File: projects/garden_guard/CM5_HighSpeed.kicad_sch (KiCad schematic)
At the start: 29 parts, among them J14 JST_SHBM04B-SRSS-TB, J2 Conn_02x07_Odd_Even, J3 Conn_01x03, J7 Micro_SD_Card_Det, J8 THD-20-R, J9 THD-02-R, SW1 Tact button, U1 TPD4EUSB30, U18 RT9742GGJ5, U2 TPD4EUSB30, U3 MagJack-A70-112-331N126

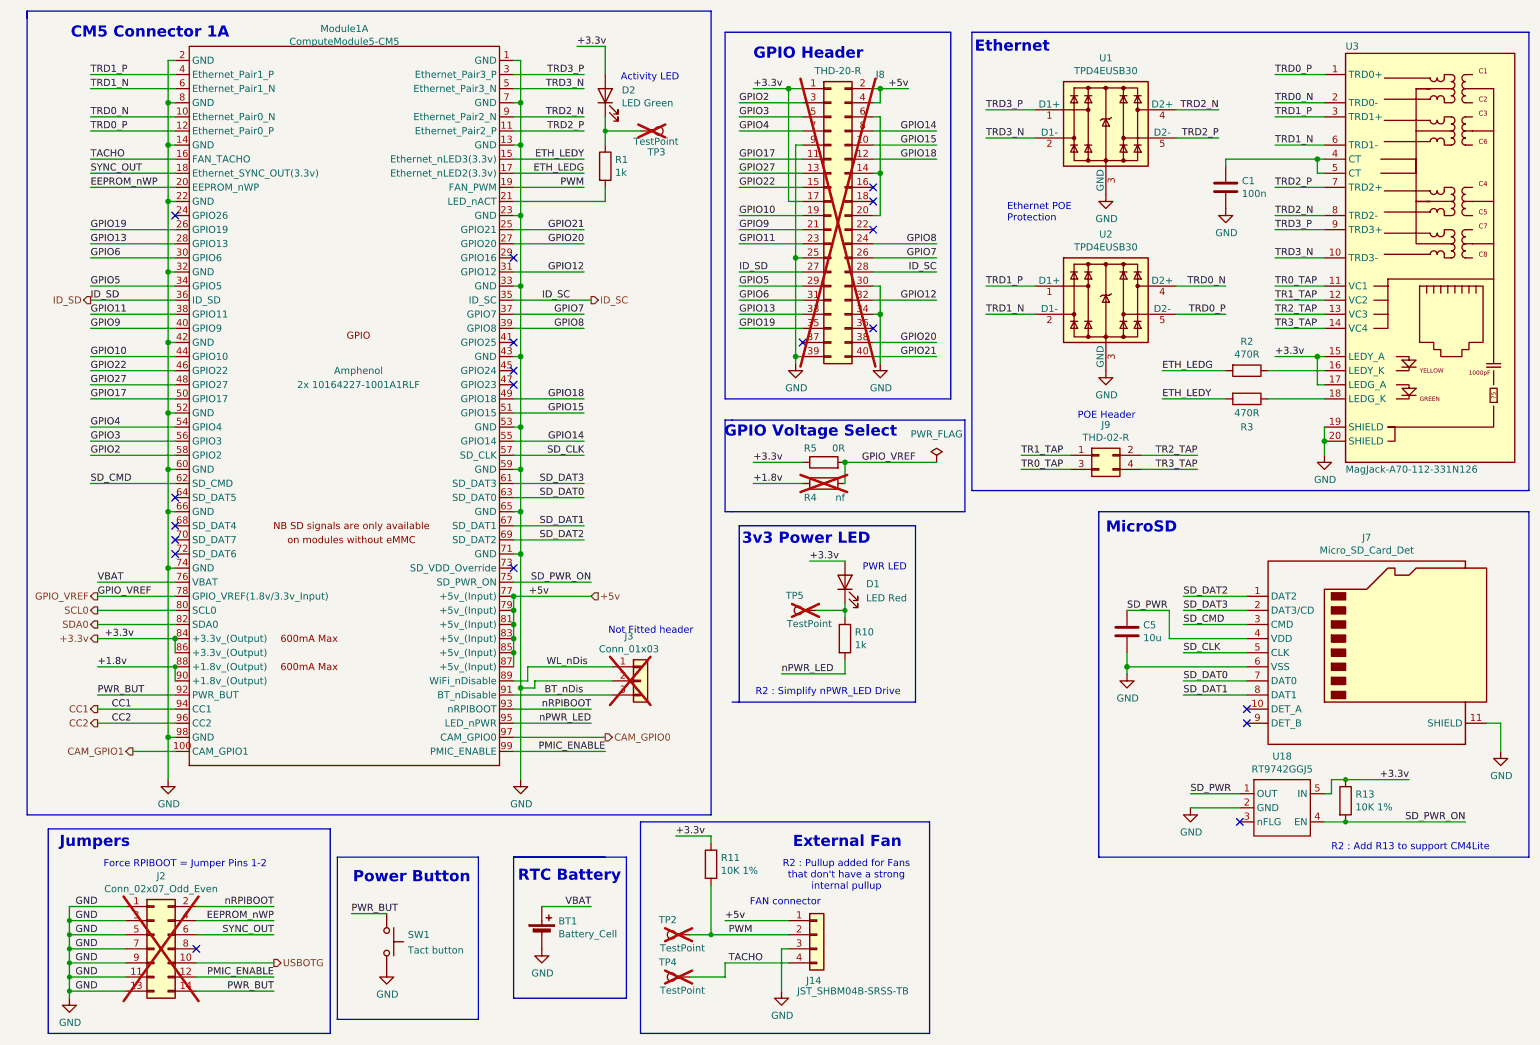
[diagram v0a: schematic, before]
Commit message: - Add PoE 12V power module - Add 12V->5V buck - Add automatic power source selection between PoE 5V and USB 5V
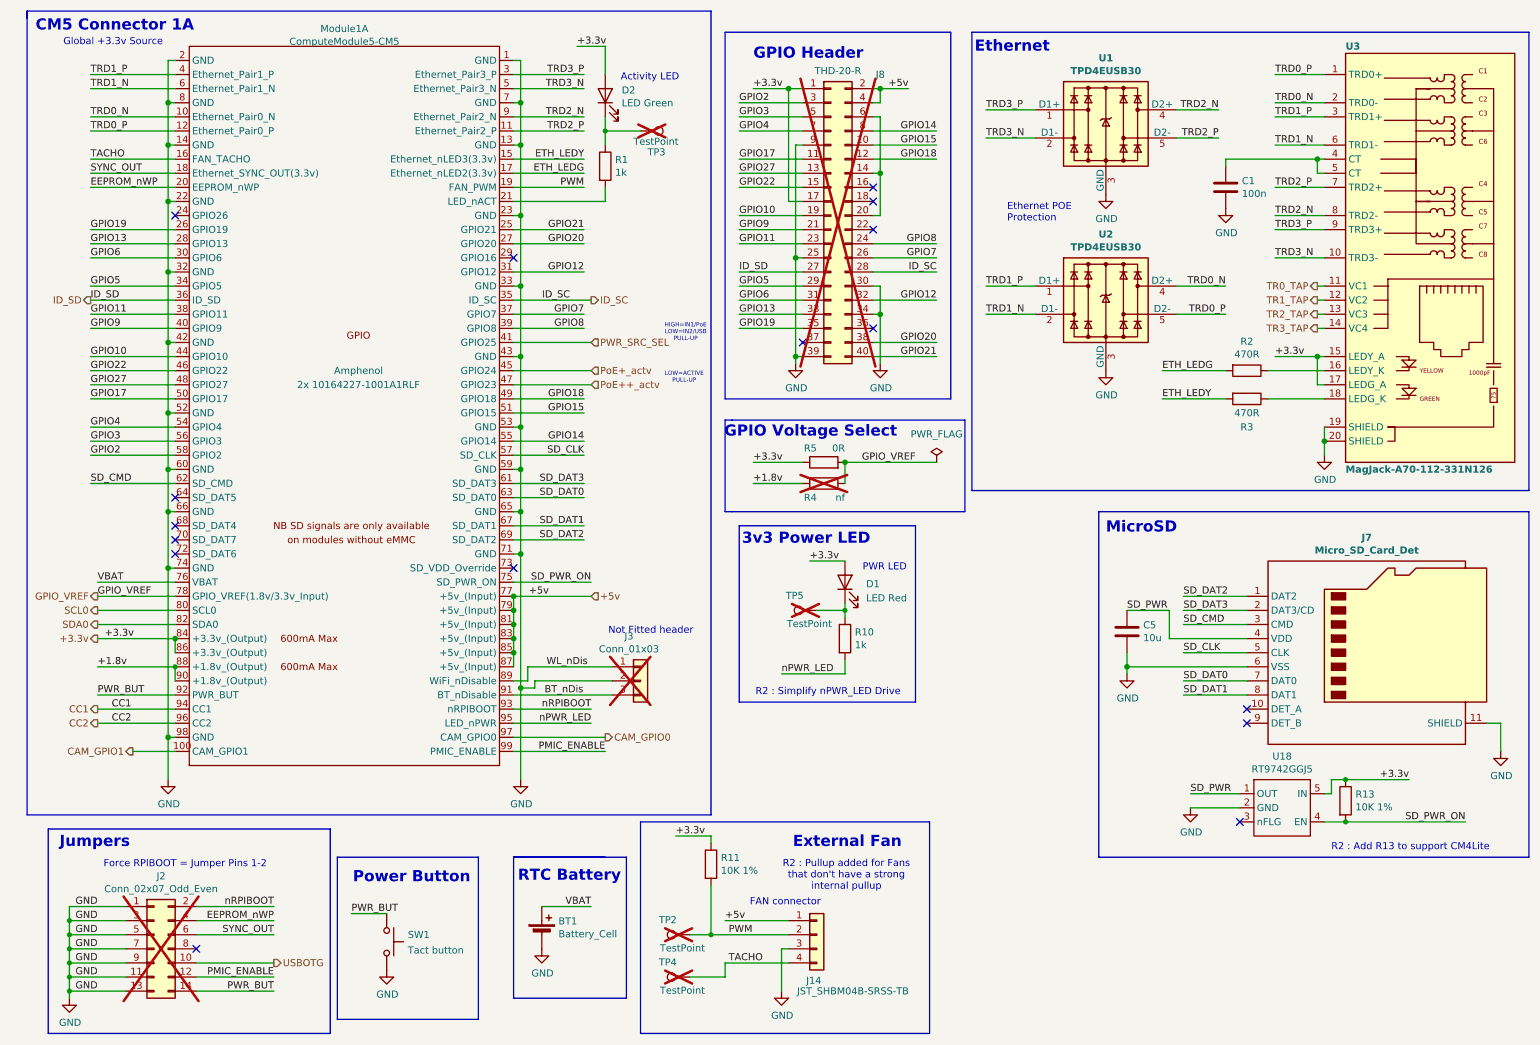
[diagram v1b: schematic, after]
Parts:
- removed J9: THD-02-R, Connector_PinHeader_2.54mm:PinHeader_2x02_P2.54mm_Vertical, symbol Connector_Generic:Conn_02x02_Odd_Even
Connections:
- net PWR_SRC_SEL: now reaches Module1.41 (GPIO25)
- net PoE+_actv: now reaches Module1.45 (GPIO24)
- net PoE++_actv: now reaches Module1.47 (GPIO23)
- no-connect marks 19 -> 16
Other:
- note added: "Global +3.3v Source"
- note added: "HIGH=IN1/PoE LOW=IN2/USB PULL-UP"
- note added: "LOW=ACTIVE PULL-UP"
- note removed: "POE Header"

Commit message: - Add 12V and 5V power sensing - Add solenoid and IR illum outputs, power expansion, an peripheral comms - General clean-up - Remove .bak files mistakenly added in previous commits - Add *.bak to .gitignore
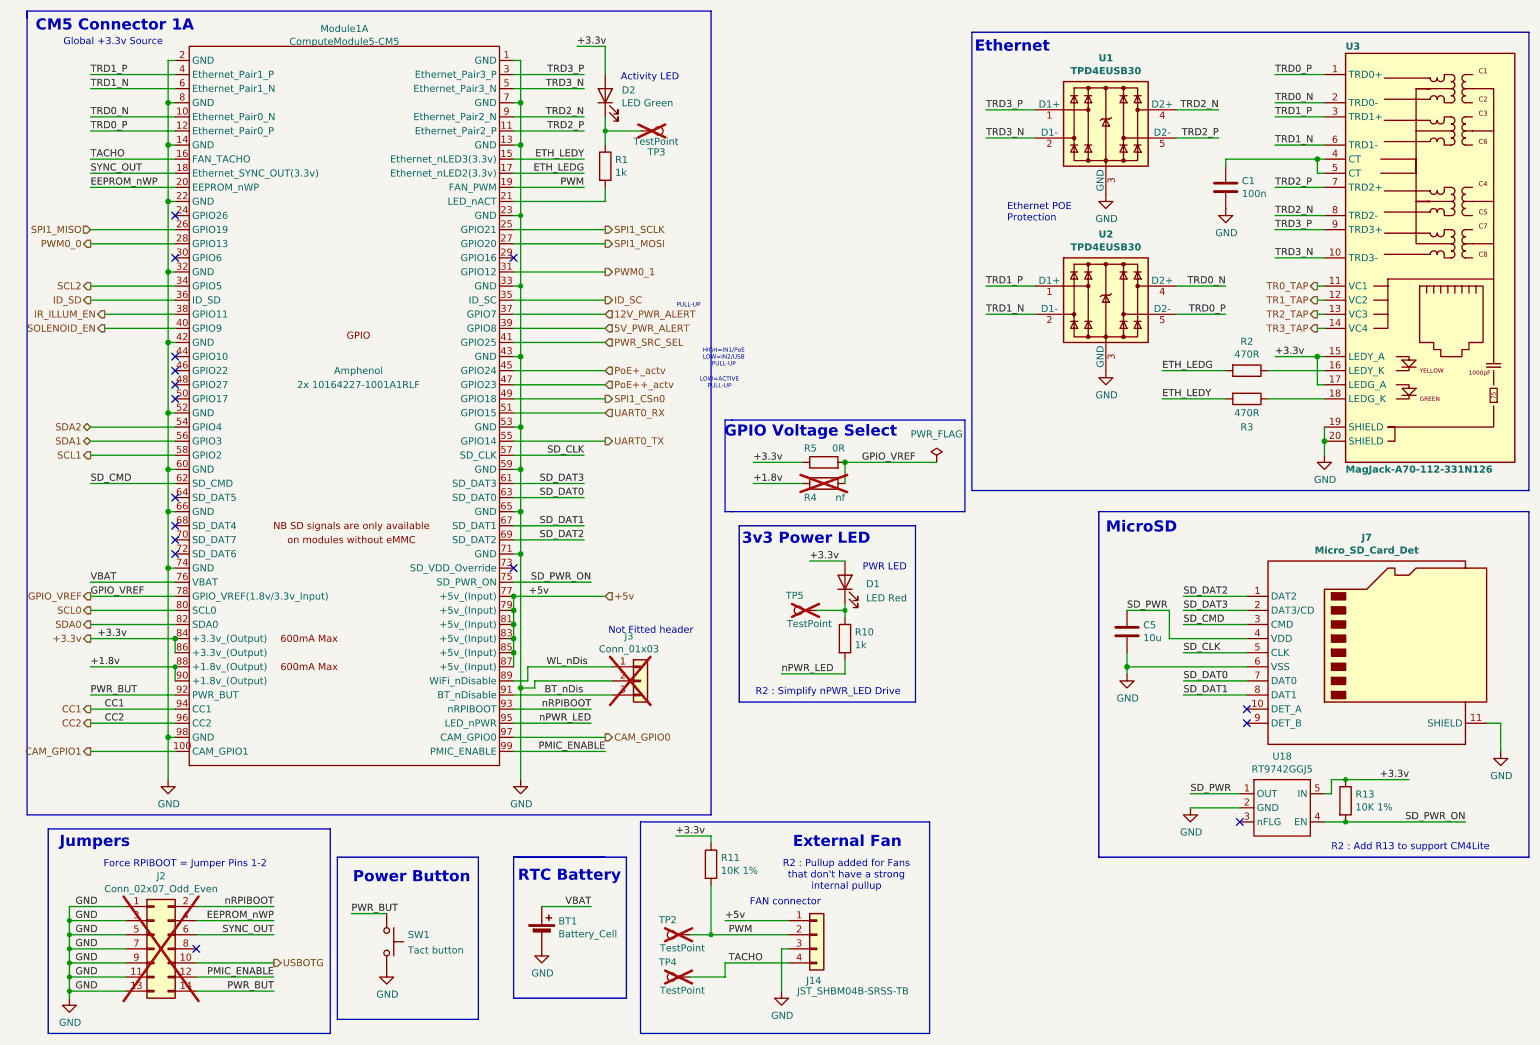
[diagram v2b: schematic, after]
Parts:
- removed J8: THD-20-R, Connector_PinHeader_2.54mm:PinHeader_2x20_P2.54mm_Vertical, symbol Connector_Generic:Conn_02x20_Odd_Even
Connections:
- net GPIO10: no longer names the net of Module1.44 (GPIO10)
- net GPIO11 renamed IR_ILLUM_EN
- net GPIO12 renamed PWM0_1
- net GPIO13 renamed PWM0_0
- net GPIO14 renamed UART0_TX
- net GPIO15 renamed UART0_RX
- net GPIO17: no longer names the net of Module1.50 (GPIO17)
- net GPIO18 renamed SPI1_CSn0
- net GPIO19 renamed SPI1_MISO
- net GPIO2 renamed SCL1
- net GPIO20 renamed SPI1_MOSI
- net GPIO21 renamed SPI1_SCLK
- net GPIO22: no longer names the net of Module1.46 (GPIO22)
- net GPIO27: no longer names the net of Module1.48 (GPIO27)
- net GPIO3 renamed SDA1
- net GPIO4 renamed SDA2
- net GPIO5 renamed SCL2
- net GPIO6: no longer names the net of Module1.30 (GPIO6)
- net GPIO7 renamed 12V_PWR_ALERT
- net GPIO8 renamed 5V_PWR_ALERT
- net GPIO9 renamed SOLENOID_EN
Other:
- note added: "PULL-UP"
- note removed: "GPIO Header"

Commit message: - Add all missing footprints - Add specific part numbers to each component in schematic
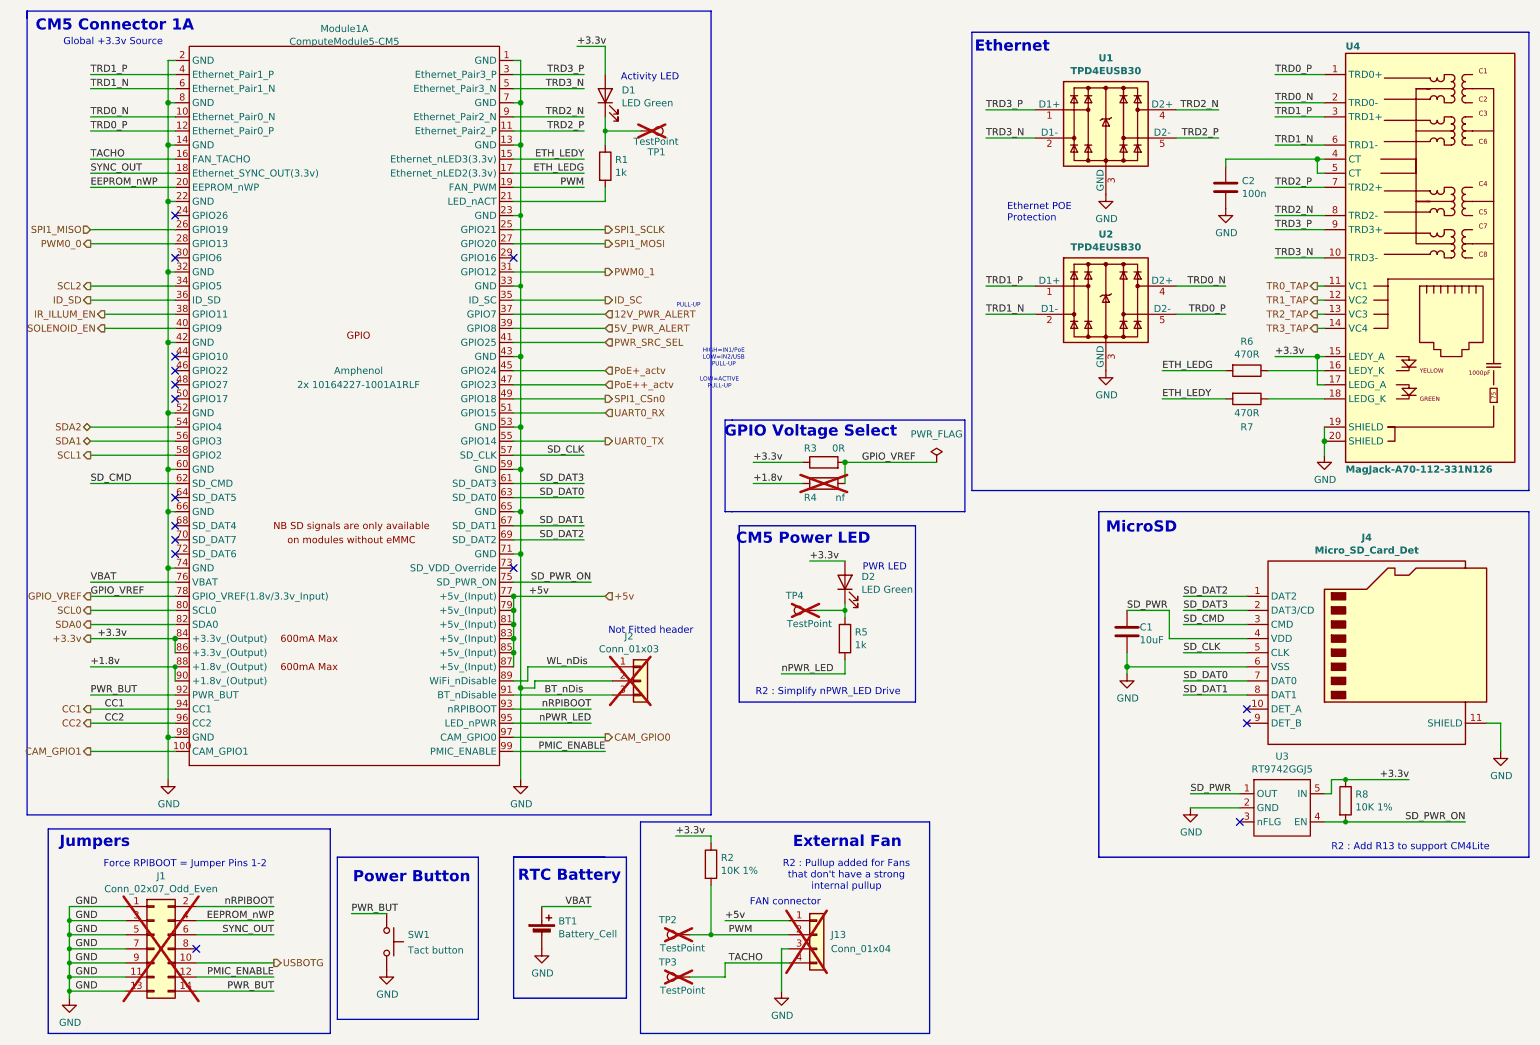
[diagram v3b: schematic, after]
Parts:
- removed D1: LED Red, symbol Device:LED
- removed J14: JST_SHBM04B-SRSS-TB, Connector_JST:JST_SH_BM04B-SRSS-TB_1x04-1MP_P1.00mm_Vertical, symbol Connector_Generic:Conn_01x04
- added D2: LED Green, LED_SMD:LED_0603_1608Metric, symbol Device:LED
- added J13: Conn_01x04, symbol Connector_Generic:Conn_01x04
- C1: renamed from C5; value 10u -> 10uF; Field6 GRM21BR71A106KA73L -> (none); Field7 Murata -> (none); MPN (none) -> GRM21BR71A106KA73L; Mfr (none) -> Murata
- D1: renamed from D2; Field5 LTST-S270KGKT -> (none); MPN (none) -> LTST-S270KGKT; Mfr (none) -> Lite-On Inc.
- renumbered C1 to C2, J2 to J1, J3 to J2, J7 to J4, R11 to R2, R5 to R3, R10 to R5, R2 to R6, R3 to R7, R13 to R8, TP3 to TP1, TP4 to TP3, TP5 to TP4, U18 to U3, U3 to U4
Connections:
- net +3.3v: now also D2.2 (A)
- net +5v: now also J13.1 (Pin_1)
- net GND: now also J13.3 (Pin_3)
- net PWM: now also J13.2 (Pin_2)
- net TACHO: now also J13.4 (Pin_4)
- net at R5.1, TP4.1: now also D2.1 (K)
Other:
- note added: "CM5 Power LED"
- note removed: "3v3 Power LED"

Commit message: - Find part numbers for CM5 parts - Minor CM5 symbol, footprint adjustments - Move to uniform small resistor and capacitor symbols - Add *lck to .gitignore
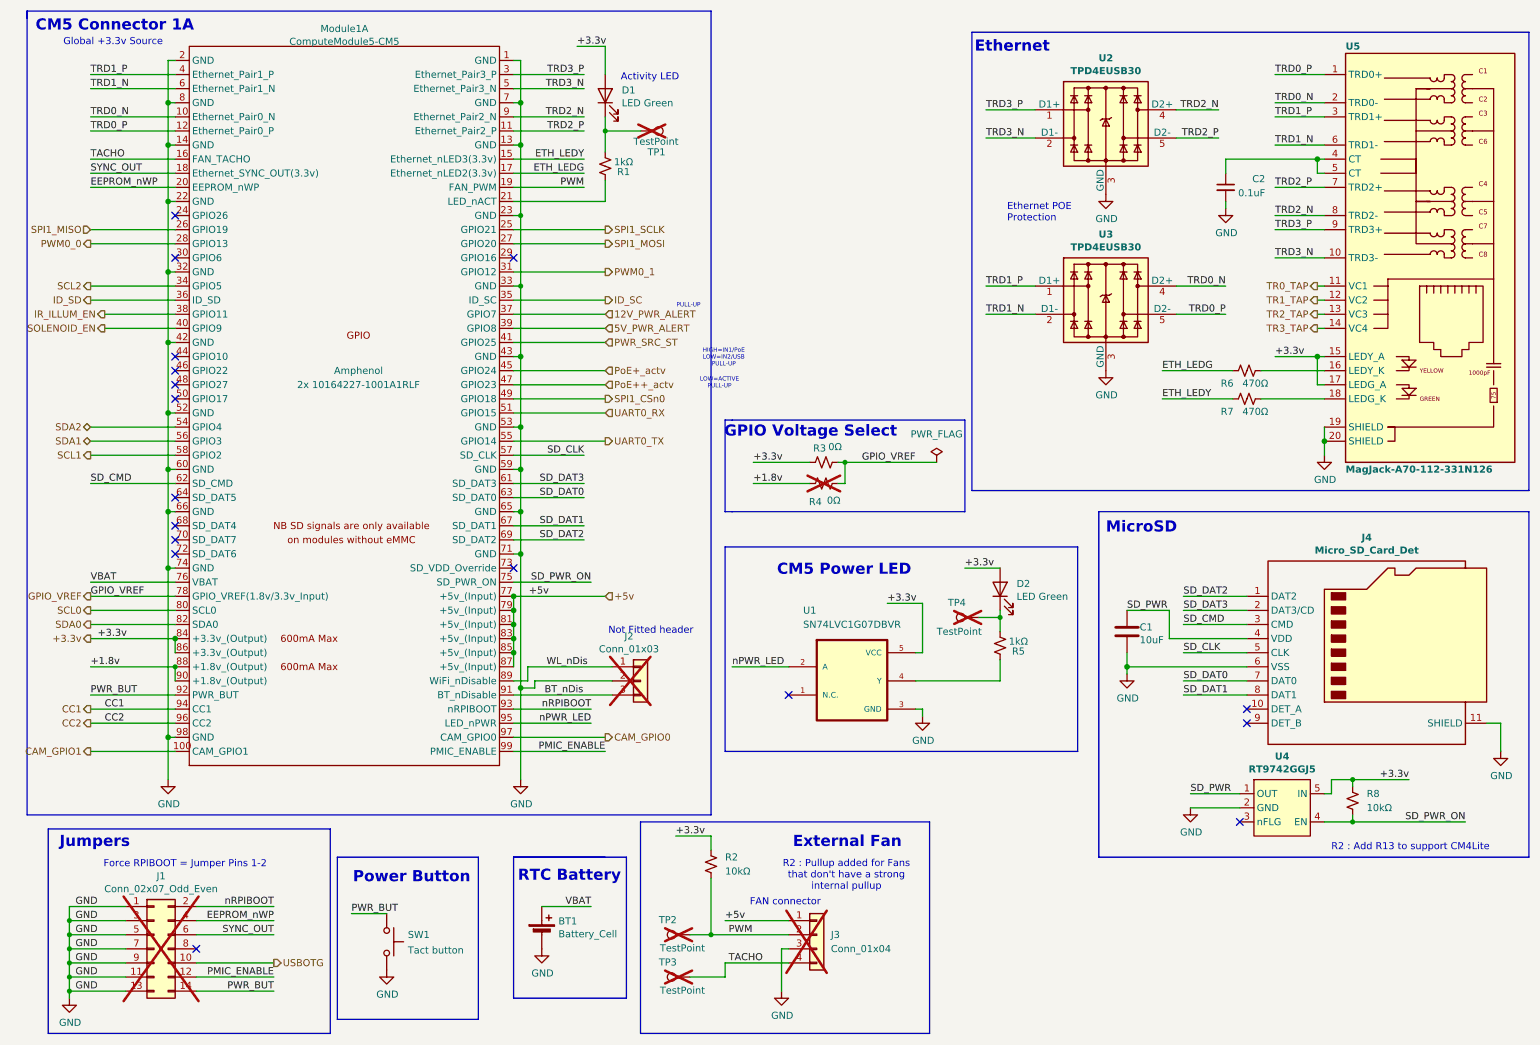
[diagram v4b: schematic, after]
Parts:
- removed C2: 100n, Capacitor_SMD:C_0402_1005Metric, symbol Device:C
- removed R1, R5: 1k, Resistor_SMD:R_0402_1005Metric, symbol Device:R
- removed R2, R8: 10K 1%, Resistor_SMD:R_0402_1005Metric, symbol Device:R
- removed R3: 0R, Resistor_SMD:R_0805_2012Metric_Pad1.20x1.40mm_HandSolder, symbol Device:R
- removed R4: nf, Resistor_SMD:R_0805_2012Metric_Pad1.20x1.40mm_HandSolder, symbol Device:R
- removed R6, R7: 470R, Resistor_SMD:R_0402_1005Metric, symbol Device:R
- added C2: 0.1uF, Resistor_SMD:R_0603_1608Metric, symbol Device:C_Small
- added R1, R5: 1kΩ, Resistor_SMD:R_0603_1608Metric, symbol Device:R_Small_US
- added R2, R8: 10kΩ, Resistor_SMD:R_0603_1608Metric, symbol Device:R_Small_US
- added R3, R4: 0Ω, Resistor_SMD:R_0603_1608Metric, symbol Device:R_Small_US
- added R6, R7: 470Ω, Resistor_SMD:R_0603_1608Metric, symbol Device:R_Small_US
- added U1: SN74LVC1G07DBVR, Custom_Switch:SN74LVC1G07DBVR, symbol Custom_Switch:SN74LVC1G07DBVR
- BT1: Digi-Key PN (none) -> 36-3034-ND; Field5 36-3034-ND -> (none); Field6 3034 -> (none); Field7 Keystone -> Keystone Electronics; MPN (none) -> 3034; Mfr (none) -> Keystone Electronics; Part Description Battery Retainer Coin, 20.0mm 1 Cell SMD (SMT) Tab -> Battery Retainer Coin, 20.0mm 1 Cell SMD (SMT) Tab
- J3: renamed from J13; footprint (none) -> Connector_PinHeader_2.54mm:PinHeader_1x04_P2.54mm_Vertical
- J4: MPN (none) -> 5033981892; Mfr (none) -> Molex
- Module1: MPN (none) -> 10164227-1004A1RLF; Mfr (none) -> Amphenol
- SW1: Field6 PTS645VH58-2LFS -> (none); Field7 CK -> (none); MPN (none) -> PTS645VH58-2LFS; Mfr (none) -> C&K
- U2: renamed from U1; MPN (none) -> TPD4EUSB30DQAR; Mfr (none) -> Texas Instruments
- U3: renamed from U2; MPN (none) -> TPD4EUSB30DQAR; Mfr (none) -> Texas Instruments
- U4: renamed from U3; MPN (none) -> RT9742GGJ5; Mfr (none) -> Richtek USA Inc.
- U5: renamed from U4; MPN (none) -> A60-112-331P4D2; Mfr (none) -> EDAC Inc.
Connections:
- net +1.8v: now also R4.1
- net +3.3v: now also R2.1, R3.1, R8.1, U1.5 (VCC)
- net ETH_LEDG: now also R6.1
- net ETH_LEDY: now also R7.1
- net GND: now also C2.2, U1.3 (GND)
- net GPIO_VREF: now also R3.2, R4.2
- net PWM: now also R2.2
- net SD_PWR_ON: now also R8.2
- net nPWR_LED: now also U1.2 (A)
- net at U5.4 (CT), U5.5 (CT): now also C2.1
- net at U5.16 (LEDY_K): now also R6.2
- net at U5.18 (LEDG_K): now also R7.2
- net at D1.1 (K), TP1.1: now also R1.1
- net at Module1.21 (LED_nACT): now also R1.2
- net at D2.1 (K), TP4.1: now also R5.1
- net PWR_SRC_SEL renamed PWR_SRC_ST
- new net: R5.2, U1.4 (Y)
- no-connect marks 16 -> 17
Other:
- note removed: "PWR LED"
- note removed: "R2 : Simplify nPWR_LED Drive"
